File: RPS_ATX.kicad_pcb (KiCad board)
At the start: 2 copper layers, 100 x 50 mm, 73 parts, among them J1 494_ON, J10 MCU_FAN, J11 PW_IN, J13 FAN_OUT, J2 494_OUT, J3 POT, J5 PS_OUT-, J6 PS_OUT+, J7 RPS_OUT-, J8 MEAS, J9 RPS_OUT+, Q2 AO3400A, Q3 AO3400A, U1 TL494, U2 Mini360, U5 LM358, U6 INA226, U7 LM7805_TO220

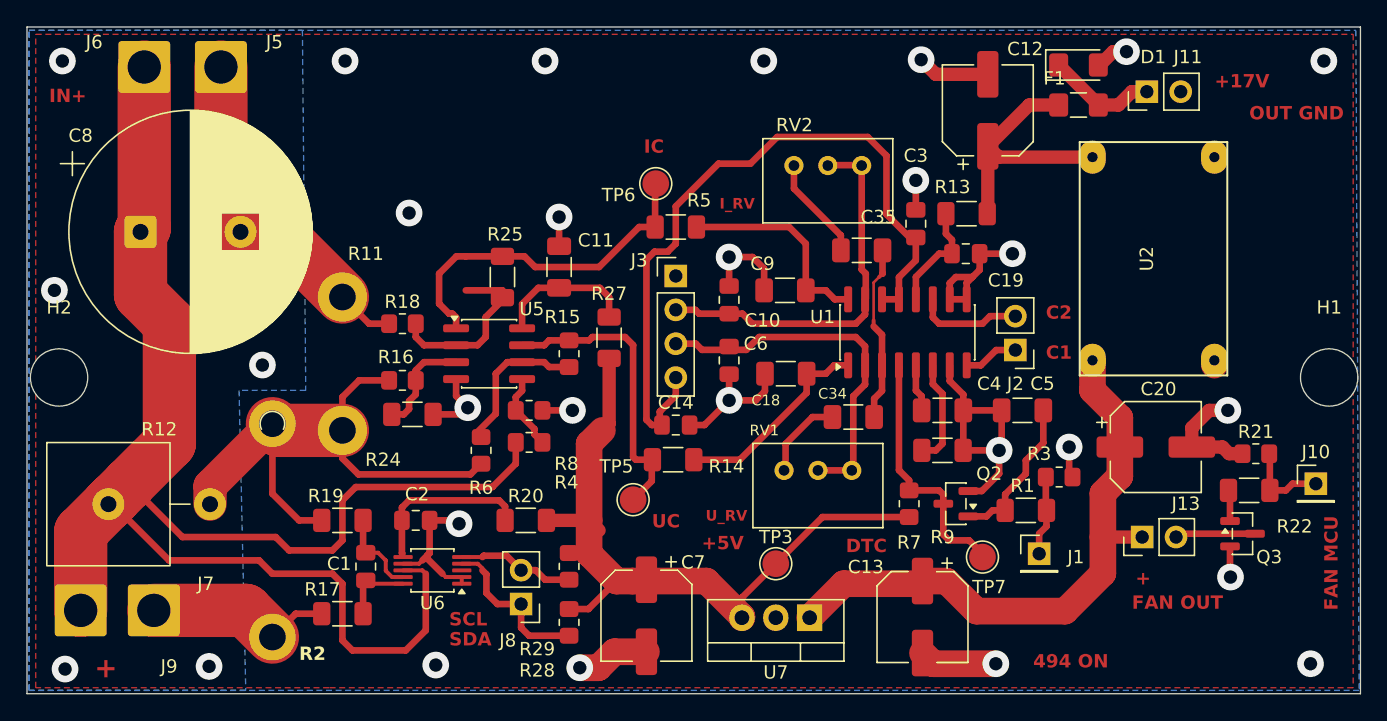
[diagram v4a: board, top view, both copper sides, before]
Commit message: +5Vref for softstart, power LED,another connectors
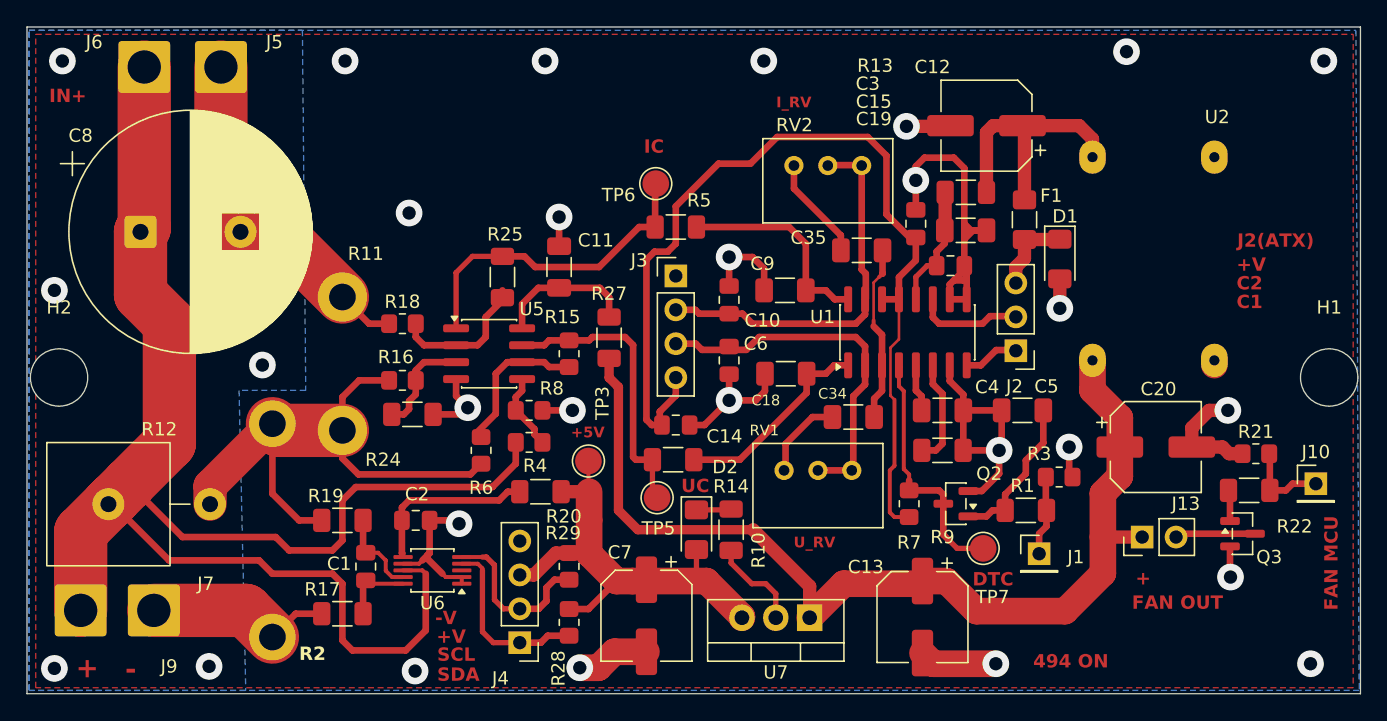
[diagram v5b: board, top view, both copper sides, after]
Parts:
- removed J11: PW_IN, Connector_PinHeader_2.54mm:PinHeader_1x02_P2.54mm_Vertical
- removed J8: MEAS, Connector_PinHeader_2.54mm:PinHeader_1x02_P2.54mm_Vertical
- added C15: 10u, Capacitor_SMD:C_1206_3216Metric_Pad1.33x1.80mm_HandSolder, F.Cu at (162.3, 87.4)
- added D2: PW_LED, LED_SMD:LED_1206_3216Metric_Pad1.42x1.75mm_HandSolder, F.Cu at (142.2, 109.8)
- added J4: MCU, Connector_PinHeader_2.54mm:PinHeader_1x04_P2.54mm_Vertical, F.Cu at (128.9, 118.3)
- added R10: 1K, Resistor_SMD:R_1206_3216Metric_Pad1.30x1.75mm_HandSolder, F.Cu at (144.8, 109.8)
- F1: value 0.5A -> 1A
- J2: value 494_OUT -> ATX; footprint Connector_PinHeader_2.54mm:PinHeader_1x02_P2.54mm_Vertical -> Connector_PinHeader_2.54mm:PinHeader_1x03_P2.54mm_Vertical
- moved TP3 16.0 mm to (134.1, 104.7)
- moved D1 14.6 mm to (169.4, 89.5), turned to -90 degrees
- moved F1 9.51 mm to (166.8, 86.6), turned to -90 degrees
- moved R20 2.42 mm to (130.4, 107.0)
- moved TP5 1.81 mm to (139.2, 107.5)
- moved R13 1.60 mm to (162.3, 84.5)
- moved C19 1.46 mm to (161.2, 90.0)
- moved C12 1.15 mm to (163.9, 79.5), turned to 180 degrees
- moved TP7 0.65 mm to (163.7, 111.2)
- moved J2 0.06 mm to (166.1, 96.4)
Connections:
- C13 pad 1: +8V -> +12V
- C20 pad 1: +8V -> +12V
- D1 pad 1: Net-(D1-K) -> +17.5V
- F1 pad 2: Net-(D1-K) -> +17.5V
- J13 pad 1: +8V -> +12V
- R27 pad 1: +5V -> +12V
- R7 pad 1: +5V -> +5V_REF
- U2 pad 4: +8V -> +12V
- U7 pad 1: +8V -> +12V
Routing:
- net +12V: track 0.00 -> 76.3 mm
- net +8V: track 45.5 -> 0.00 mm
- net +5V: track 54.0 -> 34.0 mm
- net GND: track 130.3 -> 148.6 mm
- net +5V_REF: track 55.2 -> 73.3 mm
- net Net-(D1-K): track 8.28 -> 0.00 mm
- net +17.5V: track 0.00 -> 6.19 mm
- net Net-(J4-Pin_2): track 8.84 -> 12.7 mm
- net /Analog/sh_meas_r-: track 13.5 -> 10.8 mm
- net Net-(D2-K): track 0.00 -> 2.63 mm
- net /Analog/i_op_out: track 26.4 -> 24.4 mm
- net Net-(J4-Pin_1): track 12.2 -> 13.5 mm
- net Net-(U1-VCC): track 8.30 -> 9.35 mm
- net Net-(R14-Pad1): track 22.4 -> 21.8 mm
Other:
- board text added: "+V"
- board text added: "-"
- board text added: "-V"
- board text added: "J2(ATX)"
- board text removed: "+17V"
- board text removed: "OUT GND"
